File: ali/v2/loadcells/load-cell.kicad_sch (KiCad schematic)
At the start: 4 parts

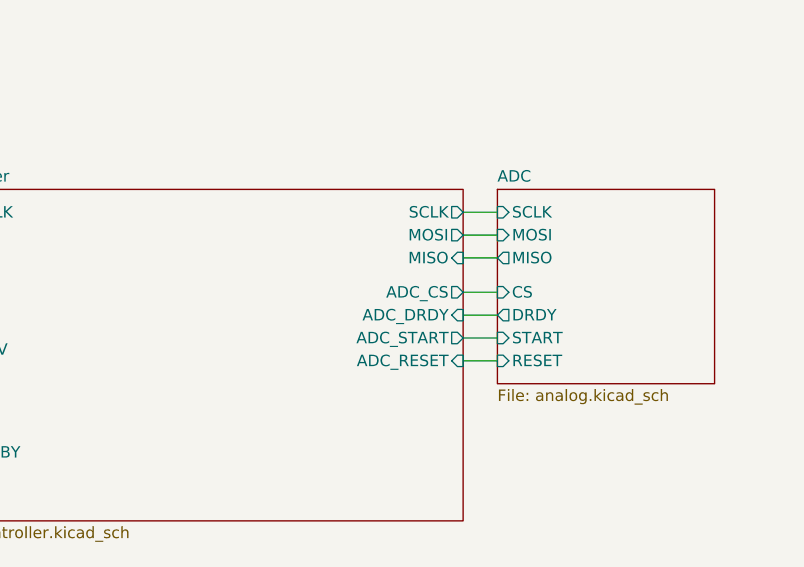
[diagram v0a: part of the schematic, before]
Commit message: Update load cells to use timer pins
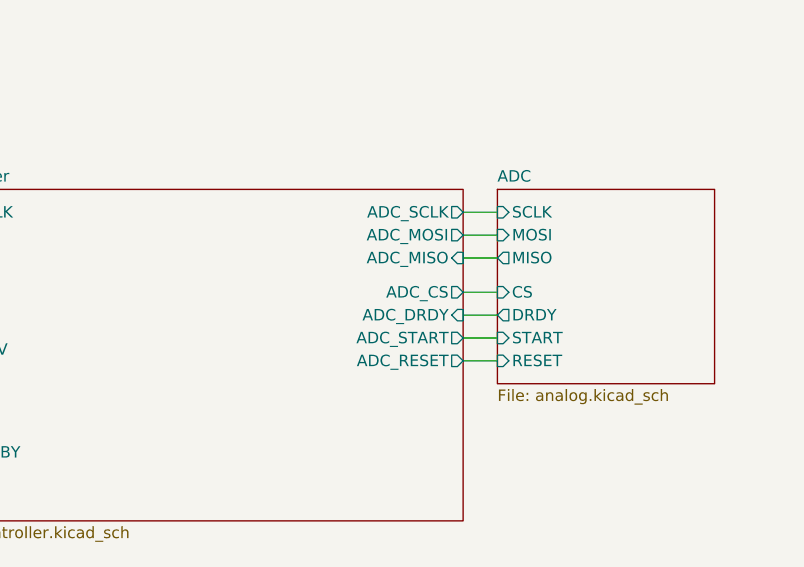
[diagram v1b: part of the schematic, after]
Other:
- sheet Microcontroller ports: added ADC_MISO, ADC_MOSI, ADC_SCLK; removed MISO, MOSI, SCLK
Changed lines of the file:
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@@
 			)
 		)
-		(pin "ADC_RESET" input
+		(pin "ADC_RESET" output
 			(at 171.45 144.78 0)
 			(effects
@@
 				)
 				(justify left)
-			)
-		)
-		(pin "MISO" input
-			(at 171.45 133.35 0)
-			(effects
-				(font
-					(size 1.27 1.27)
-				)
-				(justify right)
-			)
-		)
-		(pin "SCLK" output
-			(at 171.45 128.27 0)
-			(effects
-				(font
-					(size 1.27 1.27)
-				)
-				(justify right)
 			)
 		)
@@
 			)
 		)
-		(pin "MOSI" output
-			(at 171.45 130.81 0)
-			(effects
-				(font
-					(size 1.27 1.27)
-				)
-				(justify right)
-			)
-		)
 		(pin "ETH_~{RST}" output
 			(at 107.95 151.13 180)
@@
 			)
 		)
+		(pin "ADC_MISO" input
+			(at 171.45 133.35 0)
+			(effects
+				(font
+					(size 1.27 1.27)
+				)
+				(justify right)
+			)
+		)
+		(pin "ADC_MOSI" output
+			(at 171.45 130.81 0)
+			(effects
+				(font
+					(size 1.27 1.27)
+				)
+				(justify right)
+			)
+		)
+		(pin "ADC_SCLK" output
+			(at 171.45 128.27 0)
+			(effects
+				(font
+					(size 1.27 1.27)
+				)
+				(justify right)
+			)
+		)

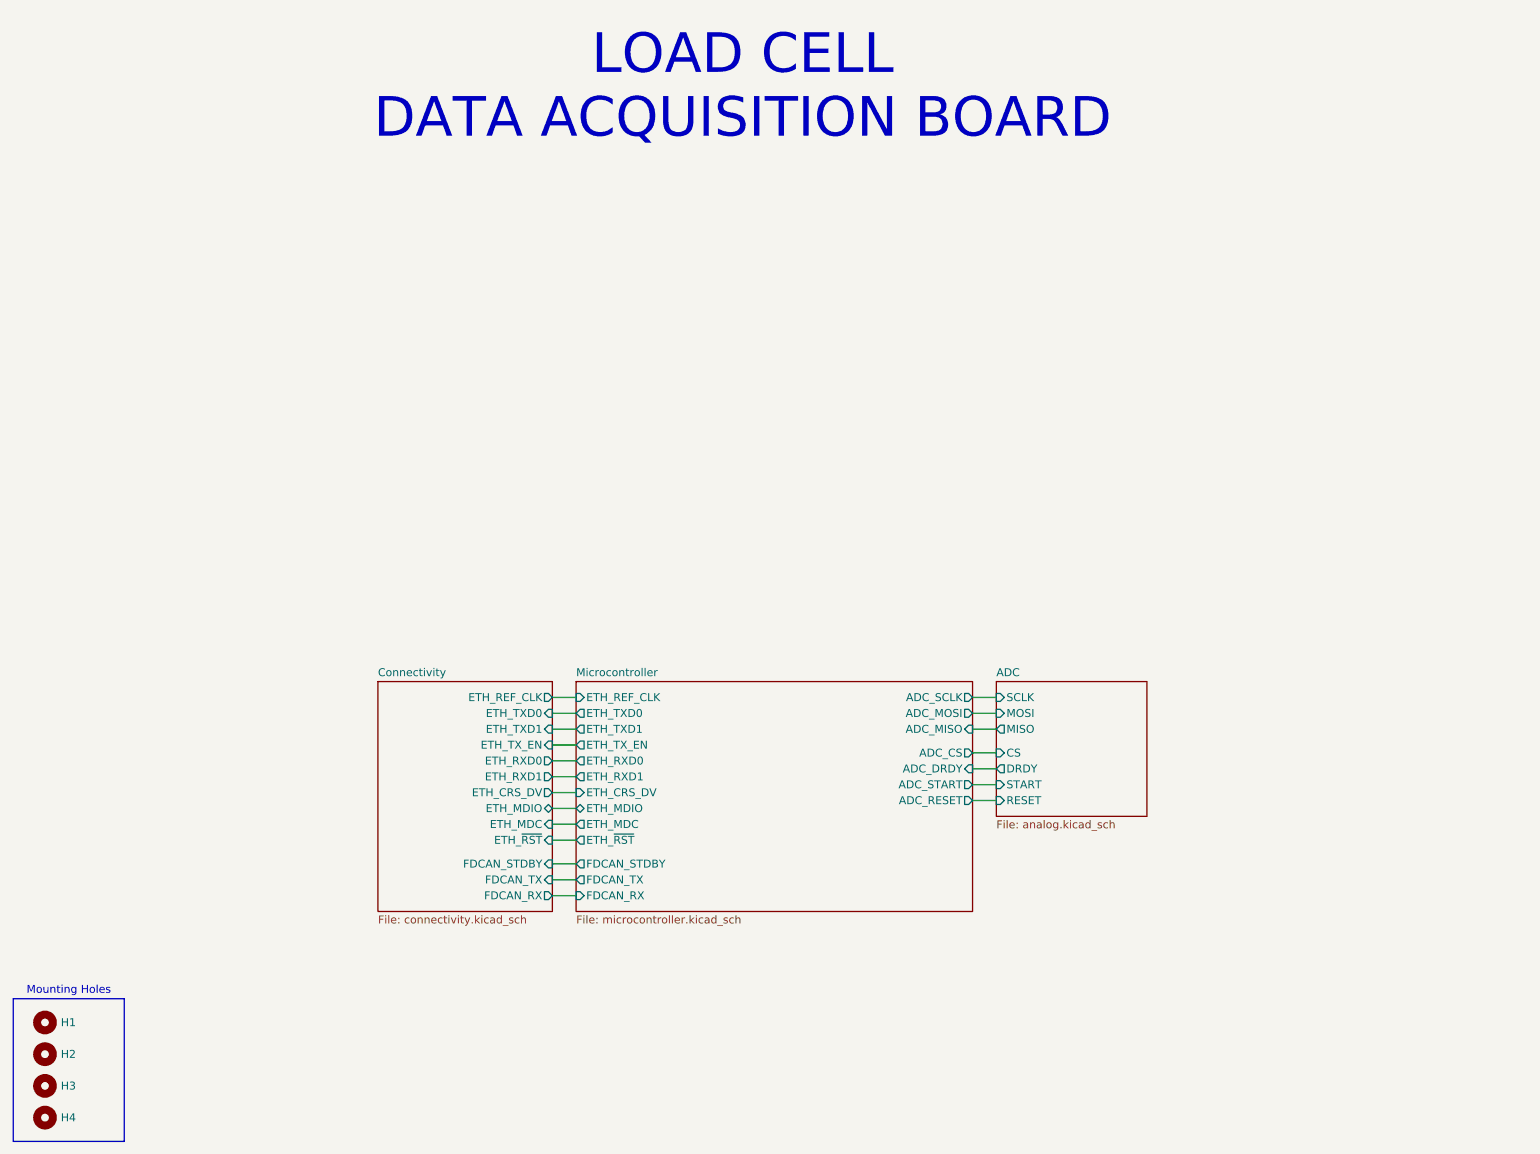
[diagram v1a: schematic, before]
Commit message: Swap to sync'd ADS1261s on LC, update README and clean up Just scripts, some frame changes too.
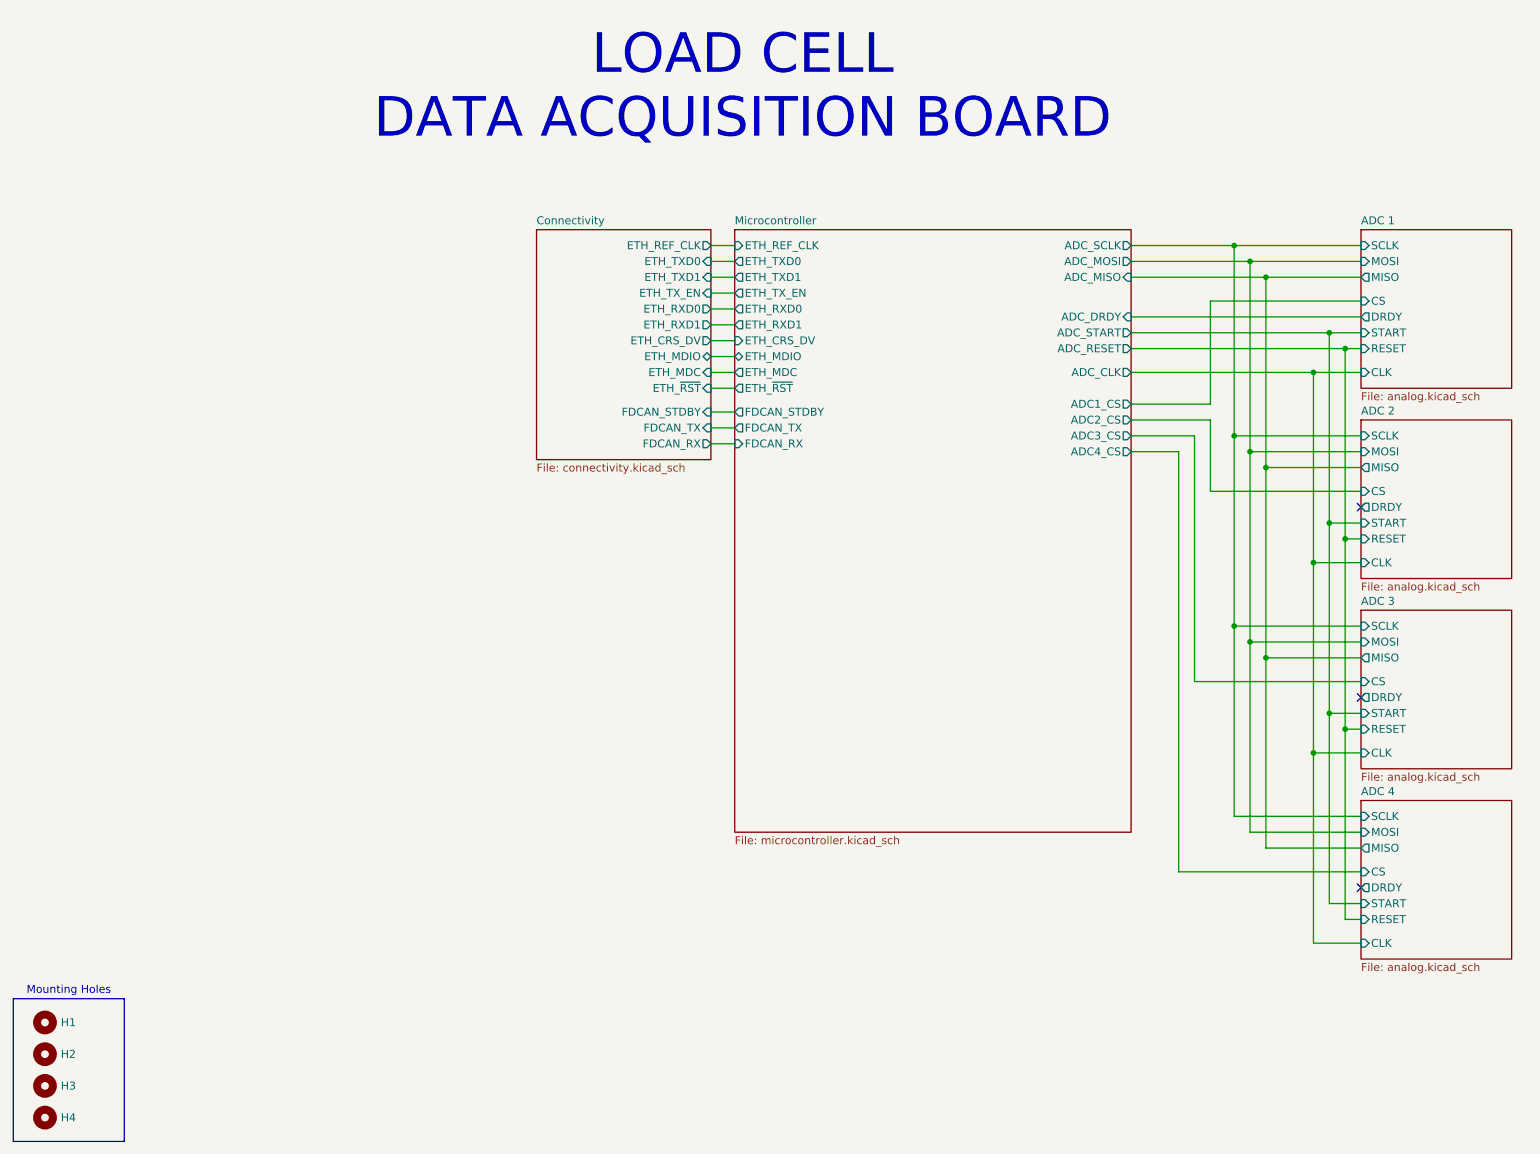
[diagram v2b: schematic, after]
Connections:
- no-connect marks 0 -> 3
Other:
- sheet ADC renamed ADC 1
- added sheet ADC 2 (analog.kicad_sch)
- added sheet ADC 3 (analog.kicad_sch)
- added sheet ADC 4 (analog.kicad_sch)
- sheet ADC 1 ports: added CLK; removed none
- sheet Microcontroller ports: added ADC1_CS, ADC2_CS, ADC3_CS, ADC4_CS, ADC_CLK; removed ADC_CS

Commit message: Globally remove LCSC labels, update MPNs and IOCs, add +5V monitoring to DAQs, fix some footprints
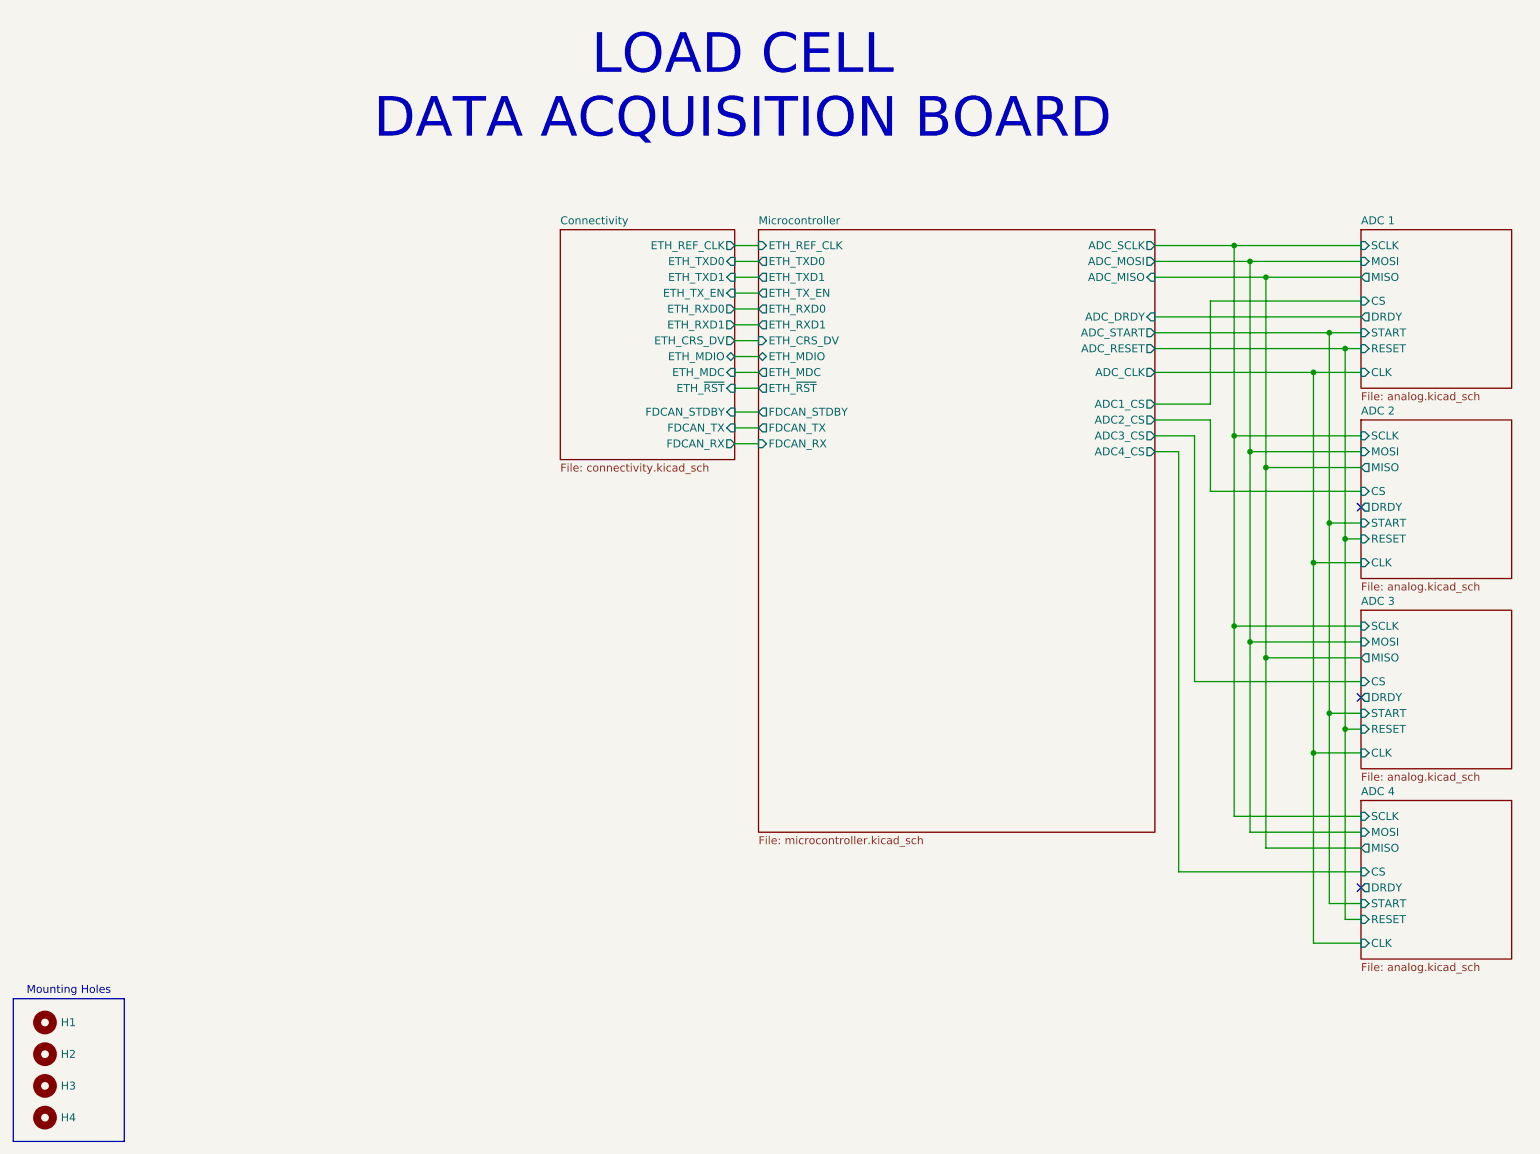
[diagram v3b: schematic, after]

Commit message: Begin prep for second board review
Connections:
- no-connect marks 3 -> 0
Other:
- sheet ADC 1 renamed ADC
- removed sheet ADC 2
- removed sheet ADC 3
- removed sheet ADC 4
- sheet ADC ports: added none; removed CLK
- sheet Microcontroller ports: added ADC_CS; removed ADC1_CS, ADC2_CS, ADC3_CS, ADC4_CS, ADC_CLK
